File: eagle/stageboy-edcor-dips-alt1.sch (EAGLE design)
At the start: 38 parts, among them IC1 MEGA8-P, IC2 7805TV, J1 POWER_JACKPTH, Q1 16MHz, X1 MIDI IN, X2 MIDI OUT, X4 22-23-2021, X6 GBIO

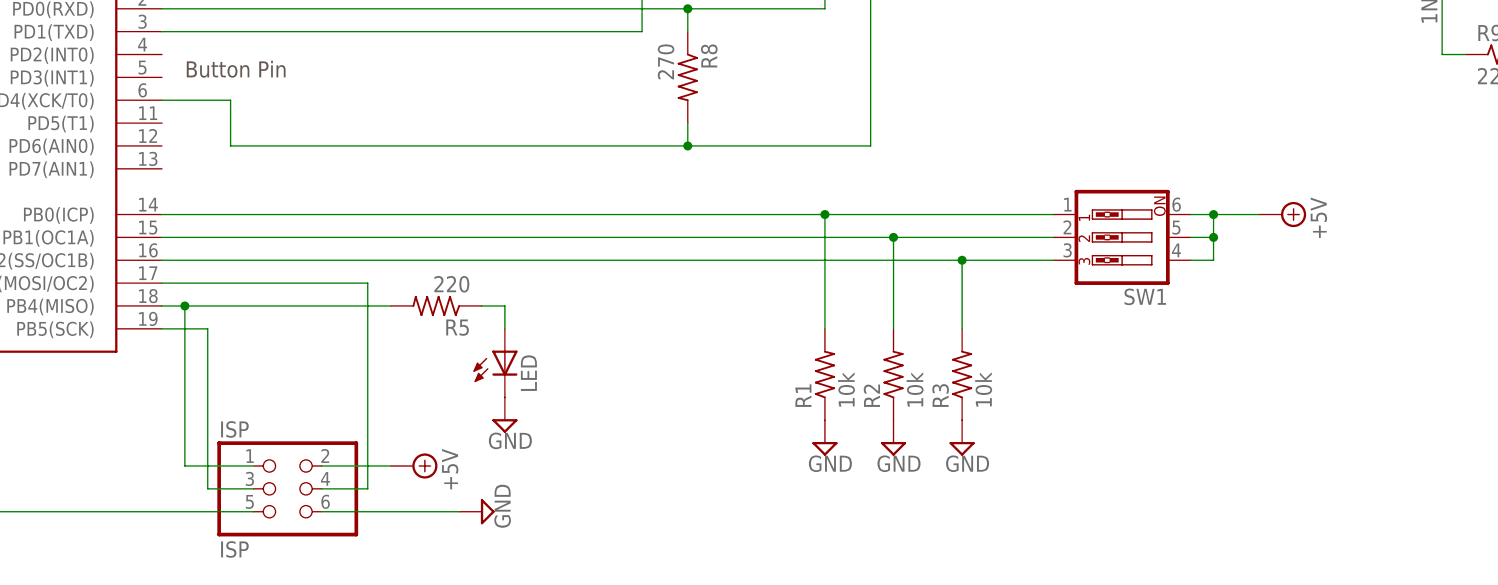
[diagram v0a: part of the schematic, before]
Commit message: Added an alternate board layout
This layout moves the AVR down further away from the analog
bits and expands the ground and power planes, while also
replacing the pull-down resistors with the internal AVR
pull-ups.
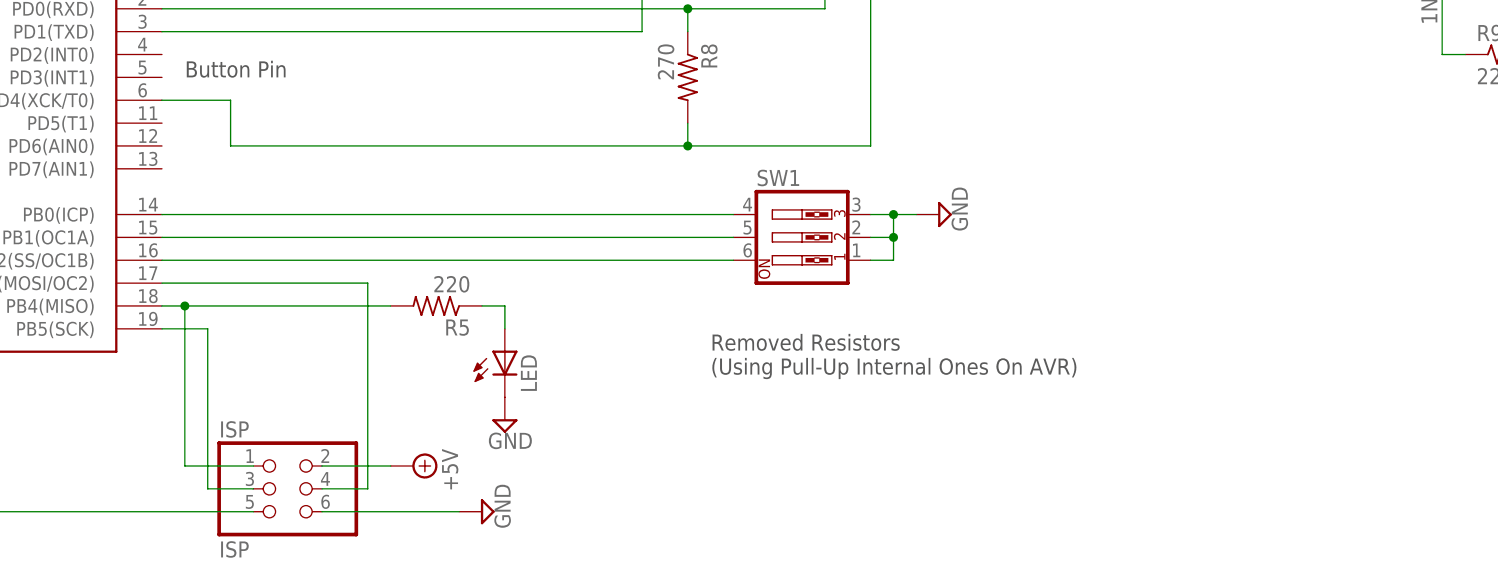
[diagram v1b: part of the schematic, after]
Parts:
- removed R1, R2, R3: 10k, resistor:R-US_0204/7
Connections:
- removed net N$14: IC1.PB1(OC1A), R2.2, SW1.2
- removed net N$15: IC1.PB2(SS/OC1B), R3.2, SW1.3
- new net N$5: IC1.PB1(OC1A), SW1.5
- new net N$6: IC1.PB2(SS/OC1B), SW1.6
- net +5V: no longer SW1.4, SW1.5, SW1.6
- net GND: now also SW1.1, SW1.2, SW1.3; no longer R1.1, R2.1, R3.1
- net N$4: now also SW1.4; no longer R1.2, SW1.1
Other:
- note added: "Removed Resistors (Using Pull-Up Internal Ones On AVR)"
- moved on the sheet: SW1
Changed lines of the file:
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@@
 <part name="C2" library="rcl" deviceset="C-US" device="025-025X050" value="100nF"/>
 <part name="SUPPLY5" library="supply2" deviceset="GND" device=""/>
-<part name="R1" library="resistor" deviceset="R-US_" device="0204/7" value="10k"/>
-<part name="R2" library="resistor" deviceset="R-US_" device="0204/7" value="10k"/>
-<part name="R3" library="resistor" deviceset="R-US_" device="0204/7" value="10k"/>
 <part name="OK1" library="optocoupler" deviceset="6N138" device=""/>
 <part name="SUPPLY8" library="supply2" deviceset="GND" device=""/>
@@
 <part name="U$1" library="EDCOR" deviceset="EDCOR-PC600/600" device=""/>
 <part name="SW1" library="special" deviceset="SW_DIP-3" device=""/>
-<part name="SUPPLY10" library="supply2" deviceset="GND" device=""/>
-<part name="SUPPLY11" library="supply2" deviceset="GND" device=""/>
-<part name="SUPPLY23" library="supply2" deviceset="GND" device=""/>
-<part name="SUPPLY25" library="supply2" deviceset="+5V" device=""/>
 <part name="LED" library="led" deviceset="LED" device="3MM"/>
 <part name="SUPPLY21" library="supply2" deviceset="GND" device=""/>
@@
 <part name="5VDC" library="con-molex" deviceset="22-23-2021" device="" value="DCPWR"/>
 <part name="J1" library="SparkFun-Connectors" deviceset="POWER_JACK" device="PTH"/>
+<part name="SUPPLY10" library="supply2" deviceset="GND" device=""/>
 </parts>
 <sheets>
@@
 <text x="241.3" y="121.92" size="1.778" layer="91">OUT</text>
 <text x="119.38" y="50.8" size="1.778" layer="97">Button Pin</text>
+<text x="177.8" y="17.78" size="1.778" layer="97">Removed Resistors
+(Using Pull-Up Internal Ones On AVR)</text>
 </plain>
 <instances>
@@
 <instance part="C2" gate="G$1" x="55.88" y="91.44"/>
 <instance part="SUPPLY5" gate="GND" x="55.88" y="96.52" rot="R180"/>
-<instance part="R1" gate="G$1" x="190.5" y="17.78" rot="R90"/>
-<instance part="R2" gate="G$1" x="198.12" y="17.78" rot="R90"/>
-<instance part="R3" gate="G$1" x="205.74" y="17.78" rot="R90"/>
 <instance part="OK1" gate="G$1" x="210.82" y="76.2" rot="R180"/>
 <instance part="SUPPLY8" gate="GND" x="195.58" y="81.28" rot="R270"/>
@@
 <instance part="SUPPLY30" gate="GND" x="2.54" y="71.12" rot="R270"/>
 <instance part="U$1" gate="G$1" x="71.12" y="205.74"/>
-<instance part="SW1" gate="A" x="223.52" y="33.02" rot="R180"/>
-<instance part="SUPPLY10" gate="GND" x="190.5" y="10.16"/>
-<instance part="SUPPLY11" gate="GND" x="198.12" y="10.16"/>
-<instance part="SUPPLY23" gate="GND" x="205.74" y="10.16"/>
-<instance part="SUPPLY25" gate="+5V" x="241.3" y="35.56" rot="R270"/>
+<instance part="SW1" gate="A" x="187.96" y="33.02"/>
 <instance part="LED" gate="G$1" x="154.94" y="20.32"/>
 <instance part="SUPPLY21" gate="GND" x="154.94" y="12.7"/>
@@
 <instance part="5VDC" gate="-2" x="101.6" y="137.16"/>
 <instance part="J1" gate="G$1" x="-12.7" y="109.22"/>
+<instance part="SUPPLY10" gate="GND" x="203.2" y="35.56" rot="R90"/>
 </instances>
 <busses>
@@
 </segment>
 <segment>
-<pinref part="R1" gate="G$1" pin="1"/>
-<pinref part="SUPPLY10" gate="GND" pin="GND"/>
-</segment>
-<segment>
-<pinref part="R2" gate="G$1" pin="1"/>
-<pinref part="SUPPLY11" gate="GND" pin="GND"/>
-</segment>
-<segment>
-<pinref part="R3" gate="G$1" pin="1"/>
-<pinref part="SUPPLY23" gate="GND" pin="GND"/>
-</segment>
-<segment>
 <pinref part="LED" gate="G$1" pin="C"/>
 <pinref part="SUPPLY21" gate="GND" pin="GND"/>
@@
 <wire x1="99.06" y1="137.16" x2="78.74" y2="137.16" width="0.1524" layer="91"/>
 <pinref part="5VDC" gate="-2" pin="S"/>
+</segment>
+<segment>
+<pinref part="SUPPLY10" gate="GND" pin="GND"/>
+<pinref part="SW1" gate="A" pin="3"/>
+<wire x1="200.66" y1="35.56" x2="198.12" y2="35.56" width="0.1524" layer="91"/>
+<pinref part="SW1" gate="A" pin="2"/>
+<wire x1="198.12" y1="35.56" x2="195.58" y2="35.56" width="0.1524" layer="91"/>
+<wire x1="195.58" y1="33.02" x2="198.12" y2="33.02" width="0.1524" layer="91"/>
+<wire x1="198.12" y1="33.02" x2="198.12" y2="35.56" width="0.1524" layer="91"/>
+<pinref part="SW1" gate="A" pin="1"/>
+<wire x1="195.58" y1="30.48" x2="198.12" y2="30.48" width="0.1524" layer="91"/>
+<wire x1="198.12" y1="30.48" x2="198.12" y2="33.02" width="0.1524" layer="91"/>
+<junction x="198.12" y="33.02"/>
+<junction x="198.12" y="35.56"/>
 </segment>
 </net>
@@
 <junction x="20.32" y="71.12"/>
 <pinref part="SUPPLY3" gate="+5V" pin="+5V"/>
-</segment>
-<segment>
-<pinref part="SW1" gate="A" pin="6"/>
-<pinref part="SUPPLY25" gate="+5V" pin="+5V"/>
-<wire x1="238.76" y1="35.56" x2="233.68" y2="35.56" width="0.1524" layer="91"/>
-<pinref part="SW1" gate="A" pin="4"/>
-<wire x1="233.68" y1="35.56" x2="231.14" y2="35.56" width="0.1524" layer="91"/>
-<wire x1="231.14" y1="30.48" x2="233.68" y2="30.48" width="0.1524" layer="91"/>
-<wire x1="233.68" y1="30.48" x2="233.68" y2="33.02" width="0.1524" layer="91"/>
-<pinref part="SW1" gate="A" pin="5"/>
-<wire x1="233.68" y1="33.02" x2="233.68" y2="35.56" width="0.1524" layer="91"/>
-<wire x1="231.14" y1="33.02" x2="233.68" y2="33.02" width="0.1524" layer="91"/>
-<junction x="233.68" y="33.02"/>
-<junction x="233.68" y="35.56"/>
 </segment>
 <segment>
@@
 </segment>
 </net>
-<net name="N$14" class="0">
-<segment>
-<pinref part="IC1" gate="G$1" pin="PB1(OC1A)"/>
-<pinref part="R2" gate="G$1" pin="2"/>
-<wire x1="116.84" y1="33.02" x2="198.12" y2="33.02" width="0.1524" layer="91"/>
-<wire x1="198.12" y1="33.02" x2="198.12" y2="22.86" width="0.1524" layer="91"/>
-<pinref part="SW1" gate="A" pin="2"/>
-<wire x1="215.9" y1="33.02" x2="198.12" y2="33.02" width="0.1524" layer="91"/>
-<junction x="198.12" y="33.02"/>
-</segment>
-</net>
-<net name="N$15" class="0">
-<segment>
-<pinref part="IC1" gate="G$1" pin="PB2(SS/OC1B)"/>
-<pinref part="R3" gate="G$1" pin="2"/>
-<wire x1="116.84" y1="30.48" x2="205.74" y2="30.48" width="0.1524" layer="91"/>
-<wire x1="205.74" y1="30.48" x2="205.74" y2="22.86" width="0.1524" layer="91"/>
-<pinref part="SW1" gate="A" pin="3"/>
-<wire x1="215.9" y1="30.48" x2="205.74" y2="30.48" width="0.1524" layer="91"/>
-<junction x="205.74" y="30.48"/>
-</segment>
-</net>
 <net name="N$17" class="0">
 <segment>
@@
 <wire x1="139.7" y1="104.14" x2="154.94" y2="104.14" width="0.1524" layer="91"/>
 <wire x1="154.94" y1="104.14" x2="154.94" y2="101.6" width="0.1524" layer="91"/>
-</segment>
-</net>
-<net name="N$4" class="0">
-<segment>
-<pinref part="IC1" gate="G$1" pin="PB0(ICP)"/>
-<pinref part="R1" gate="G$1" pin="2"/>
-<wire x1="190.5" y1="22.86" x2="190.5" y2="35.56" width="0.1524" layer="91"/>
-<wire x1="190.5" y1="35.56" x2="116.84" y2="35.56" width="0.1524" layer="91"/>
-<pinref part="SW1" gate="A" pin="1"/>
-<wire x1="215.9" y1="35.56" x2="190.5" y2="35.56" width="0.1524" layer="91"/>
-<junction x="190.5" y="35.56"/>
 </segment>
 </net>
@@
 </segment>
 </net>
+<net name="N$4" class="0">
+<segment>
+<pinref part="IC1" gate="G$1" pin="PB0(ICP)"/>
+<pinref part="SW1" gate="A" pin="4"/>
+<wire x1="116.84" y1="35.56" x2="180.34" y2="35.56" width="0.1524" layer="91"/>
+</segment>
+</net>
+<net name="N$5" class="0">
+<segment>
+<pinref part="SW1" gate="A" pin="5"/>
+<pinref part="IC1" gate="G$1" pin="PB1(OC1A)"/>
+<wire x1="180.34" y1="33.02" x2="116.84" y2="33.02" width="0.1524" layer="91"/>
+</segment>
+</net>
+<net name="N$6" class="0">
+<segment>
+<pinref part="IC1" gate="G$1" pin="PB2(SS/OC1B)"/>
+<pinref part="SW1" gate="A" pin="6"/>
+<wire x1="116.84" y1="30.48" x2="180.34" y2="30.48" width="0.1524" layer="91"/>
+</segment>
+</net>
 </nets>
 </sheet>
@@
 </schematic>
 </drawing>
+<compatibility>
+<note version="6.3" minversion="6.2.2" severity="warning">
+Since Version 6.2.2 text objects can contain more than one line,
+which will not be processed correctly with this version.
+</note>
+</compatibility>
 </eagle>
